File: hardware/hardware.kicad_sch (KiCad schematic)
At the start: 6 parts, among them J2 RFShield_OnePiece, J6 RFShield_OnePiece

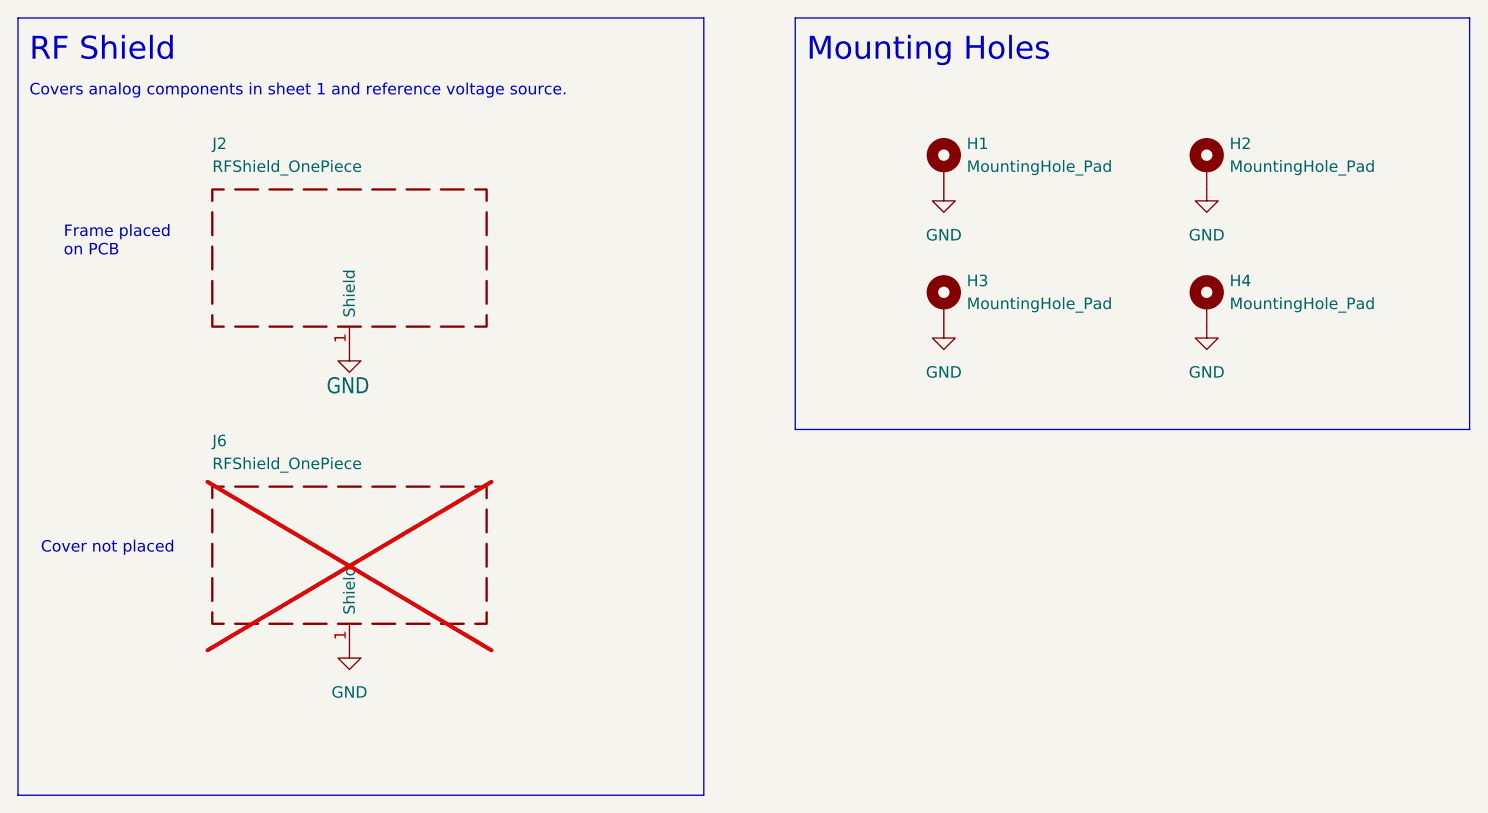
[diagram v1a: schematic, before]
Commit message: replace mini with module
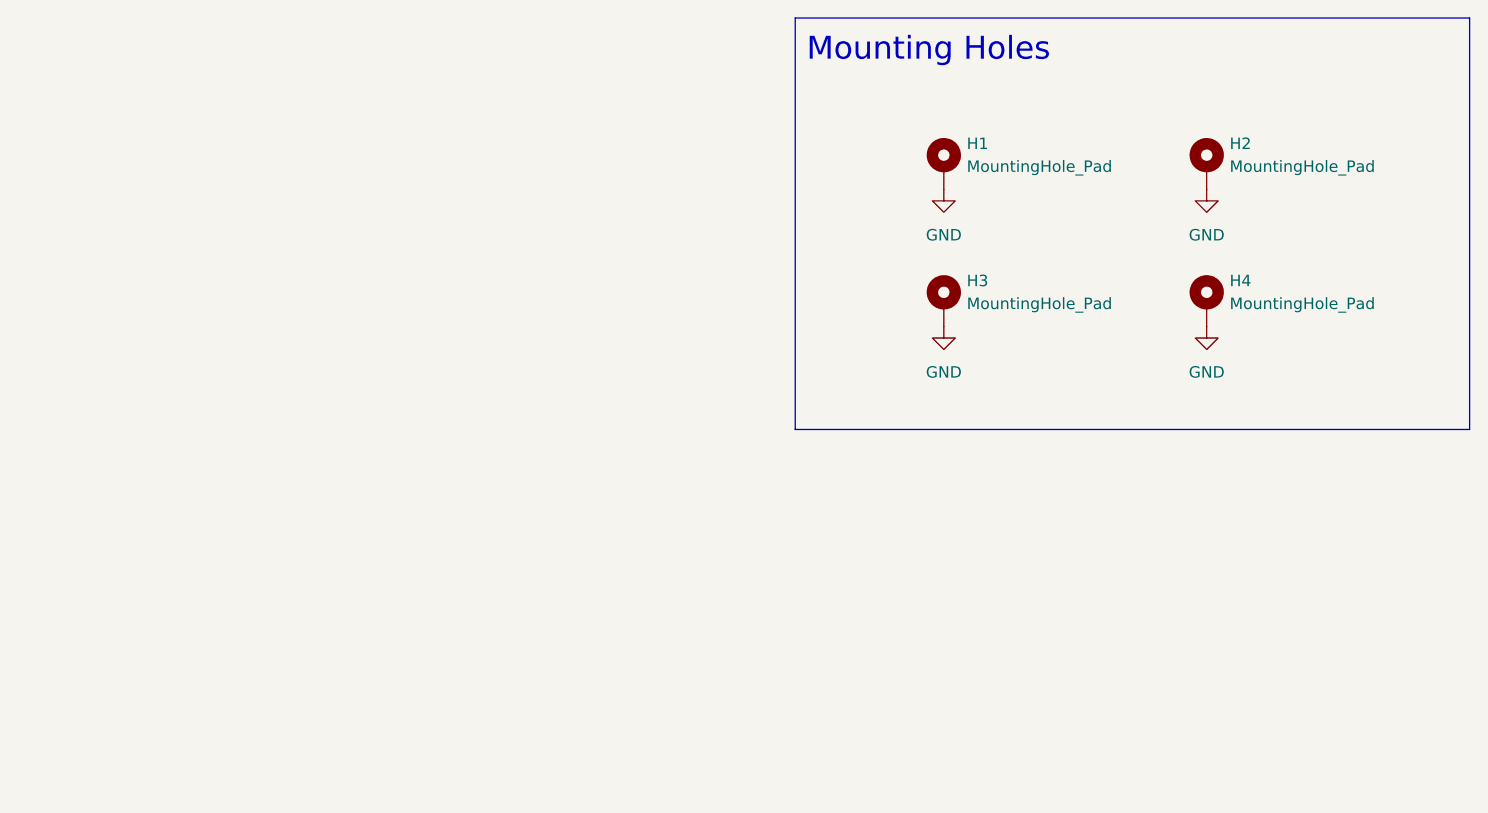
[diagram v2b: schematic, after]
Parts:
- removed J2: RFShield_OnePiece, RF_Shielding:Wuerth_36103305_30x30mm, symbol Device:RFShield_OnePiece
- removed J6: RFShield_OnePiece, symbol Device:RFShield_OnePiece
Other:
- note removed: "Cover not placed"
- note removed: "Covers analog components in sheet 1 and reference voltage source."
- note removed: "Frame placed on PCB"
- note removed: "RF Shield"
